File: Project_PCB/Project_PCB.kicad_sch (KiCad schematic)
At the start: 41 parts, among them J1 USB_C_Receptacle, J2 Myoware Connector, J3 Conn_01x02, SW1 SW_Push, SW2 SW_SPST, U1 ESP32-S3-WROOM-1, U2 RT9080-33GJ5, U3 MCP73831T-2ACI/OT, U4 MAX17048G+

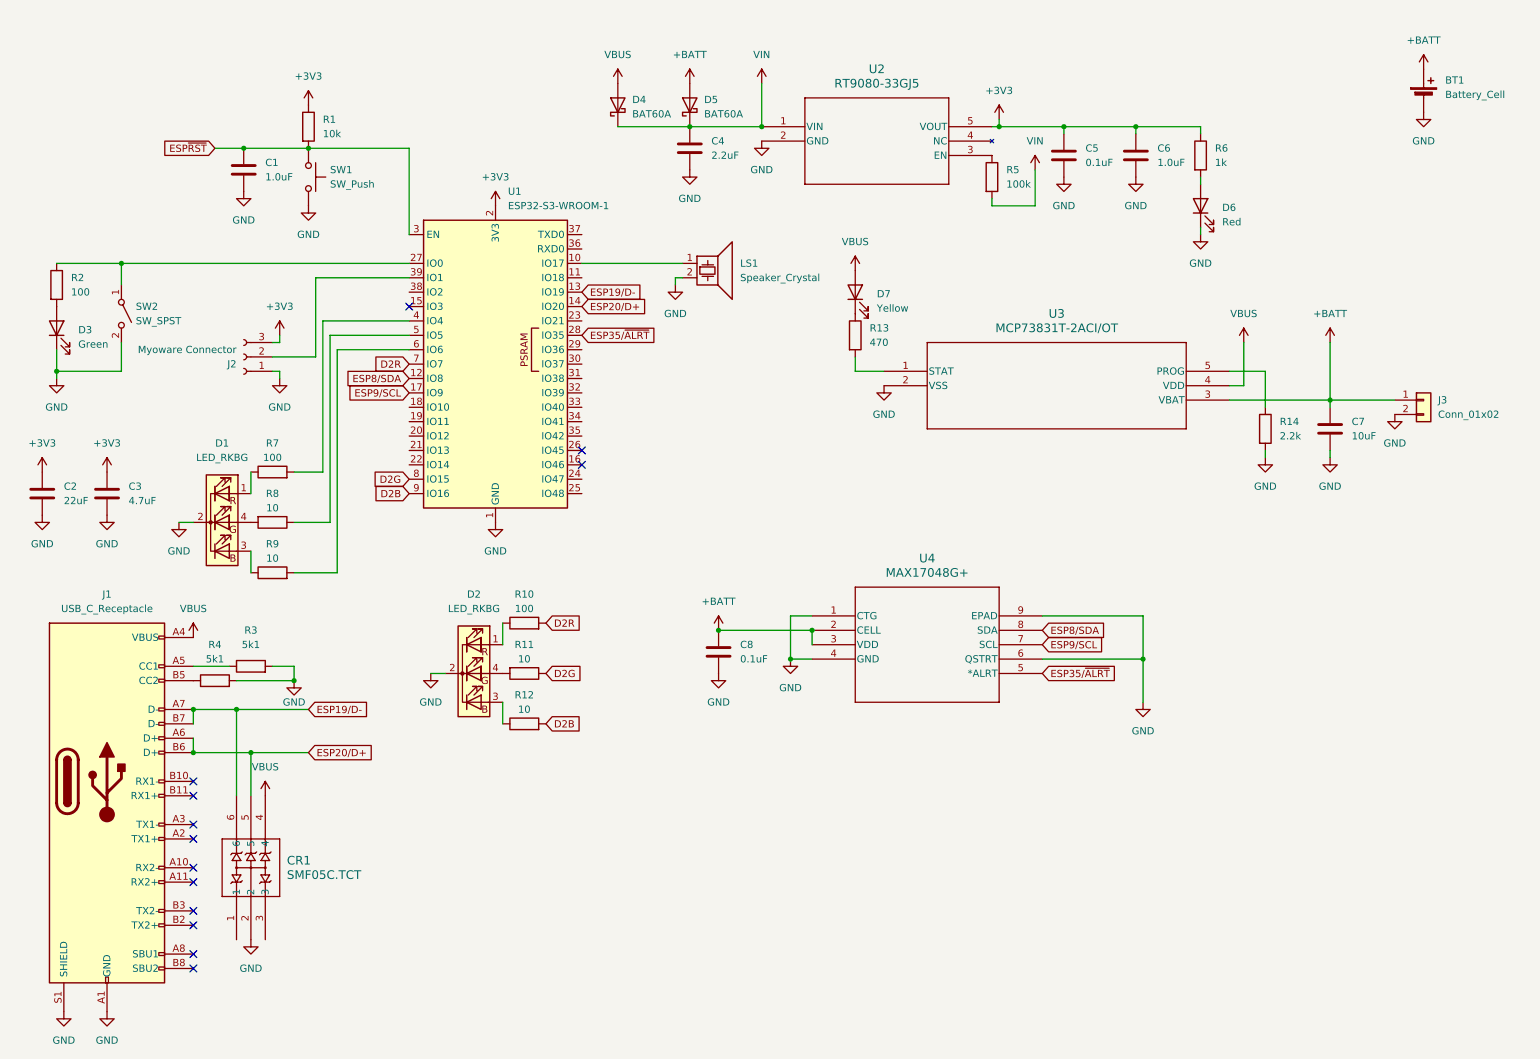
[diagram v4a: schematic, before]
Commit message: Made recommended changes, added some footprints
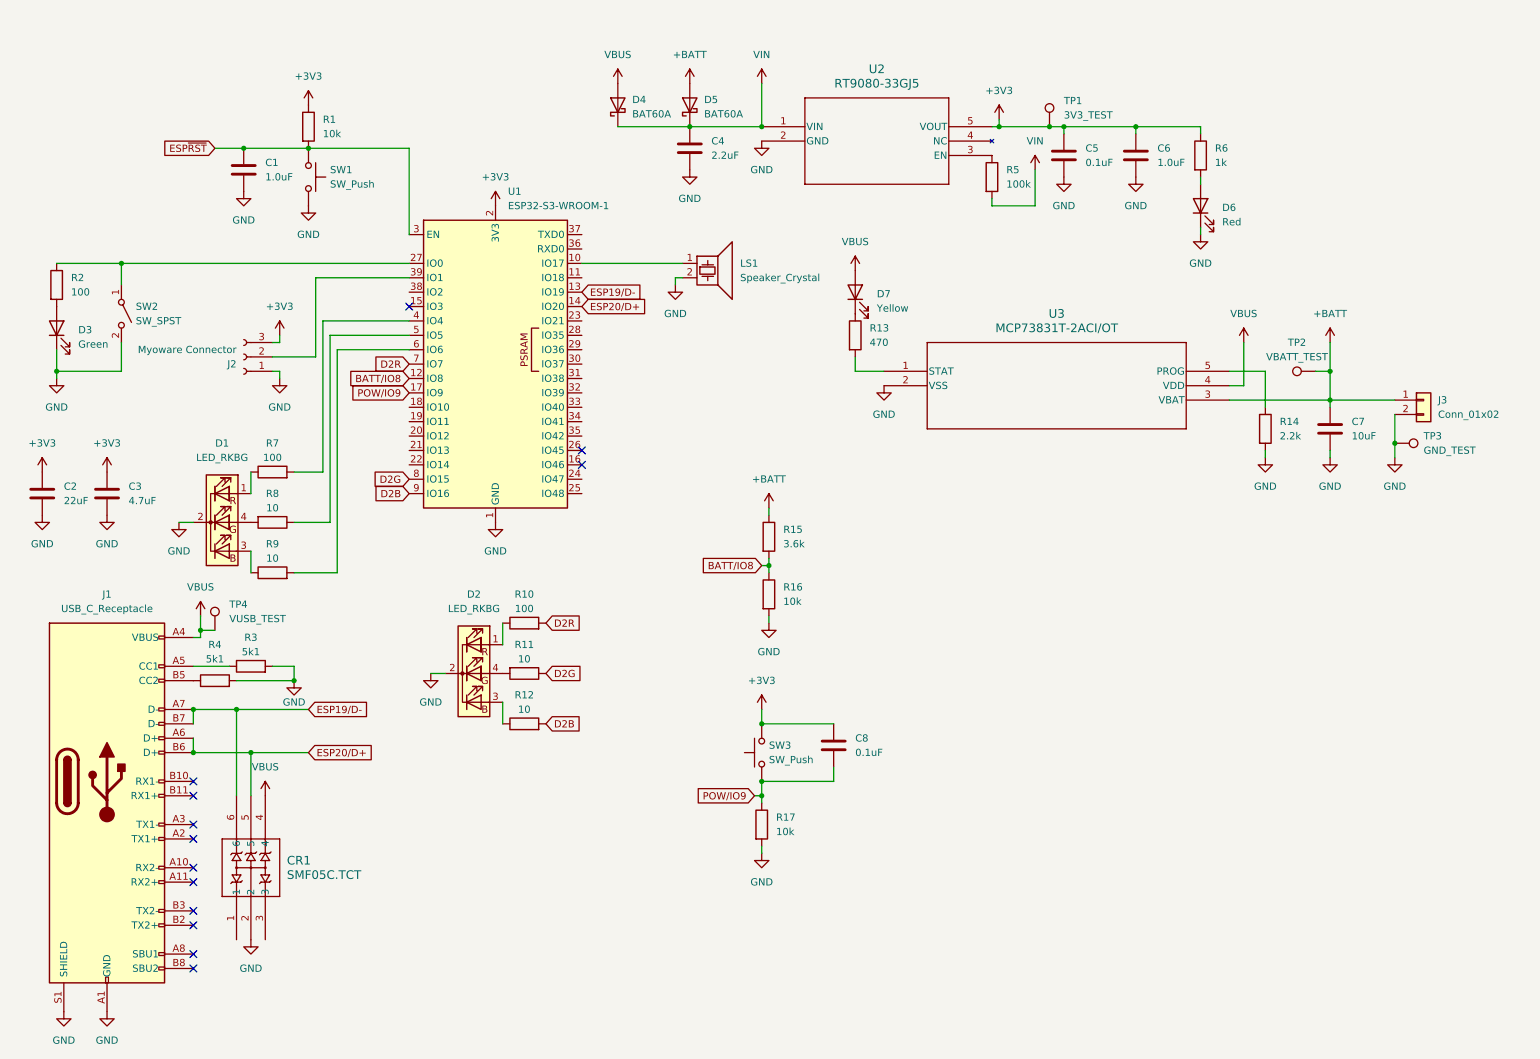
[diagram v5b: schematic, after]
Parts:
- removed BT1: Battery_Cell, symbol Device:Battery_Cell
- removed U4: MAX17048G+, 21-0168_T822+3_MXM, symbol MAX17048G:MAX17048G+
- added R15: 3.6k, Resistor_SMD:R_0603_1608Metric_Pad0.98x0.95mm_HandSolder, symbol Device:R
- added R16, R17: 10k, Resistor_SMD:R_0603_1608Metric_Pad0.98x0.95mm_HandSolder, symbol Device:R
- added SW3: SW_Push, symbol Switch:SW_Push
- added TP1: 3V3_TEST, symbol Connector:TestPoint
- added TP2: VBATT_TEST, symbol Connector:TestPoint
- added TP3: GND_TEST, symbol Connector:TestPoint
- added TP4: VUSB_TEST, symbol Connector:TestPoint
- C1, C5, C6, C8: footprint (none) -> Capacitor_SMD:C_0603_1608Metric_Pad1.08x0.95mm_HandSolder
- CR1: footprint SC70-6L_SEM -> SMF05C:SC70-6L_SEM
- D1, D2: footprint (none) -> LED_THT:LED_D5.0mm-4_RGB
- D3, D6, D7: footprint (none) -> LED_SMD:LED_0805_2012Metric_Pad1.15x1.40mm_HandSolder
- R1, R10, R11, R12, R13, R14, R2, R3, R4, R5, R6, R7, R8, R9: footprint (none) -> Resistor_SMD:R_0603_1608Metric_Pad0.98x0.95mm_HandSolder
- SW1: footprint (none) -> Button_Switch_THT:SW_PUSH_6mm
- U2: footprint TSOT-23-5_RIT -> RT9080:TSOT-23-5_RIT
- U3: footprint SOT-23-5_MC_MCH -> MCP73831:SOT-23-5_MC_MCH
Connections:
- net +3V3: now also C8.1, SW3.2, TP1.1
- net +BATT: now also R15.1, TP2.1; no longer C8.1
- net GND: now also R16.2, R17.2, TP3.1; no longer C8.2
- net VBUS: now also TP4.1
- net ESP35/~{ALRT}: no longer names the net of U1.28 (IO35)
- net ESP8/SDA renamed BATT/IO8
- net BATT/IO8: now also R15.2, R16.1
- net ESP9/SCL renamed POW/IO9
- net POW/IO9: now also C8.2, R17.1, SW3.1

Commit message: Finalized schematic, assigned all footprints
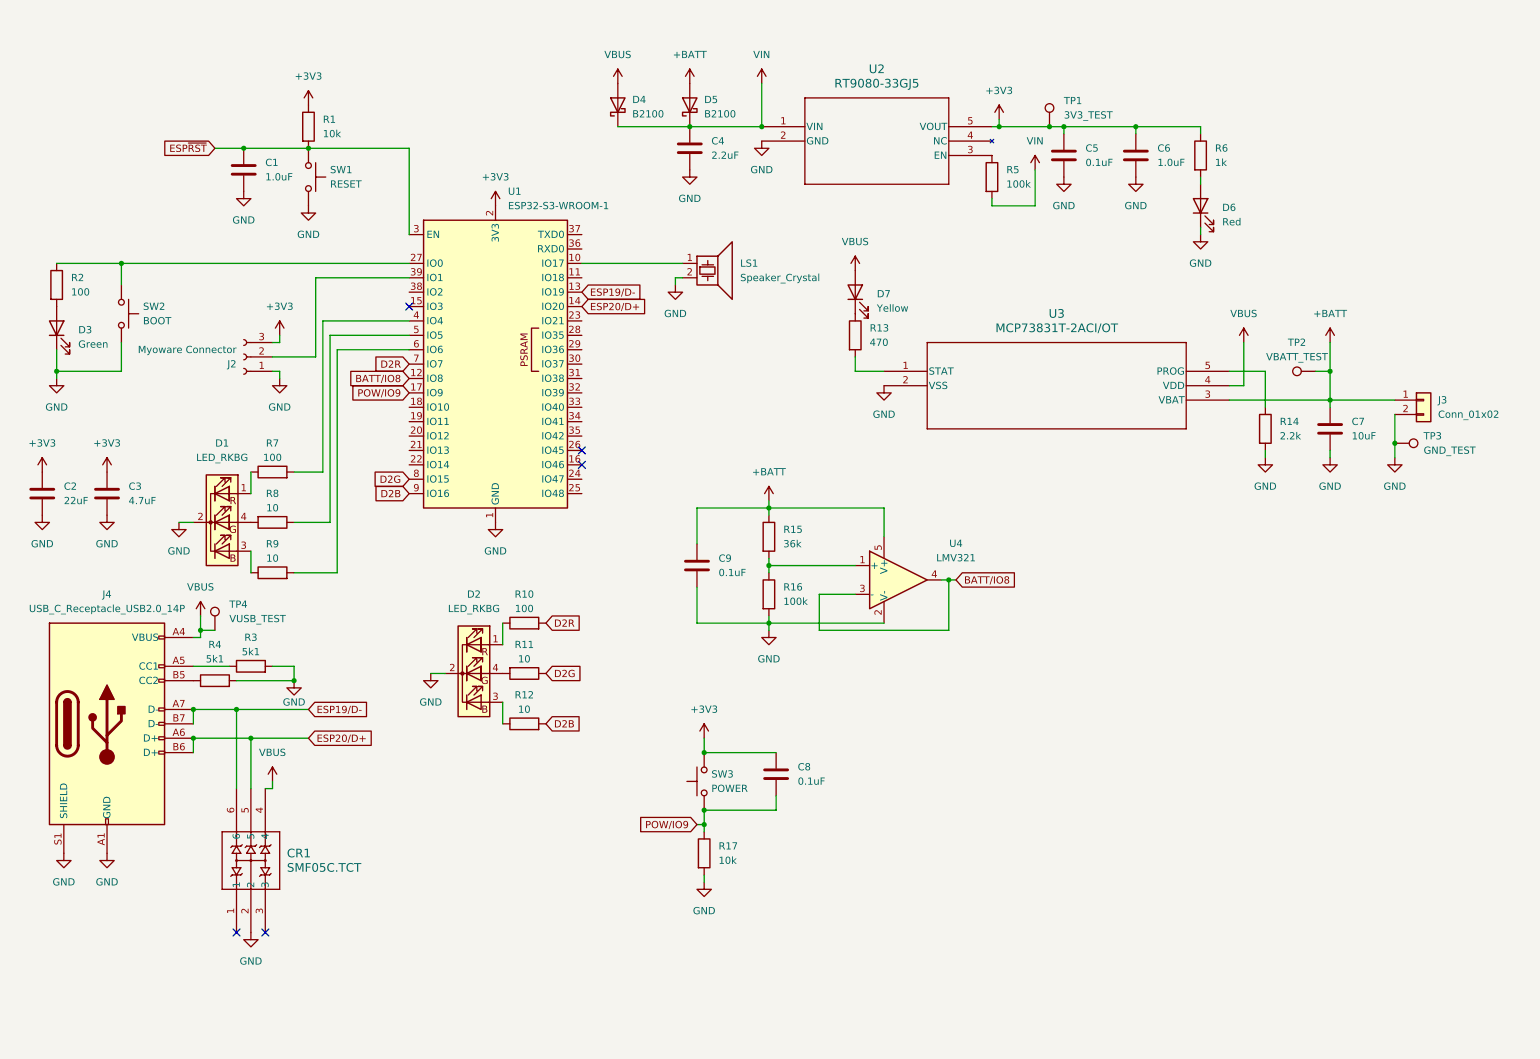
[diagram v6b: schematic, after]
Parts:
- removed D4, D5: BAT60A, Diode_SMD:D_SOD-323, symbol Diode:BAT60A
- removed J1: USB_C_Receptacle, symbol Connector:USB_C_Receptacle
- removed SW2: SW_SPST, symbol Switch:SW_SPST
- added C9: 0.1uF, Capacitor_SMD:C_0603_1608Metric_Pad1.08x0.95mm_HandSolder, symbol Device:C
- added D4, D5: B2100, Diode_SMD:D_SMB_Handsoldering, symbol Device:D_Schottky
- added J4: USB_C_Receptacle_USB2.0_14P, Connector_PinHeader_2.54mm:PinHeader_1x08_P2.54mm_Vertical, symbol Connector:USB_C_Receptacle_USB2.0_14P
- added SW2: BOOT, Button_Switch_SMD:SW_Push_1P1T_NO_CK_KSC6xxJ, symbol Switch:SW_Push
- added U4: LMV321, Package_TO_SOT_SMD:SOT-353_SC-70-5_Handsoldering, symbol Amplifier_Operational:LMV321
- C2: footprint (none) -> Capacitor_THT:C_Radial_D6.3mm_H7.0mm_P2.50mm
- C3, C4, C7: footprint (none) -> Capacitor_THT:C_Radial_D5.0mm_H11.0mm_P2.00mm
- J2: footprint (none) -> Connector_PinHeader_2.54mm:PinHeader_1x03_P2.54mm_Vertical
- LS1: footprint (none) -> LD-BZPN-1705:LDBZPN1705
- R15: value 3.6k -> 36k
- R16: value 10k -> 100k
- SW1: value SW_Push -> RESET; footprint Button_Switch_THT:SW_PUSH_6mm -> Button_Switch_SMD:SW_SPST_PTS647_Sx38
- SW3: value SW_Push -> POWER; footprint (none) -> Connector_PinHeader_2.54mm:PinHeader_1x02_P2.54mm_Vertical
- TP1, TP2, TP3, TP4: footprint (none) -> TestPoint:TestPoint_THTPad_D2.0mm_Drill1.0mm
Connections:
- net +BATT: now also C9.1, D5.2 (A), U4.5 (V+)
- net BATT/IO8: now also U4.3 (-), U4.4; no longer R15.2, R16.1
- net ESP19/D-: now also J4.A7 (D-), J4.B7 (D-)
- net ESP20/D+: now also J4.A6 (D+), J4.B6 (D+)
- net GND: now also C9.2, J4.A1 (GND), J4.A12 (GND), J4.B1 (GND), J4.B12 (GND), J4.S1 (SHIELD), SW2.2, U4.2 (V-)
- net VBUS: now also D4.2 (A), J4.A4 (VBUS), J4.A9 (VBUS), J4.B4 (VBUS), J4.B9 (VBUS)
- net VIN: now also D4.1 (K), D5.1 (K)
- net at R4.1: now also J4.B5 (CC2)
- net at R2.1, U1.27 (IO0): now also SW2.1
- net at R3.1: now also J4.A5 (CC1)
- new net: R15.2, R16.1, U4.1 (+)
- no-connect marks 13 -> 5
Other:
- moved on the sheet: C8, CR1, R17, SW3

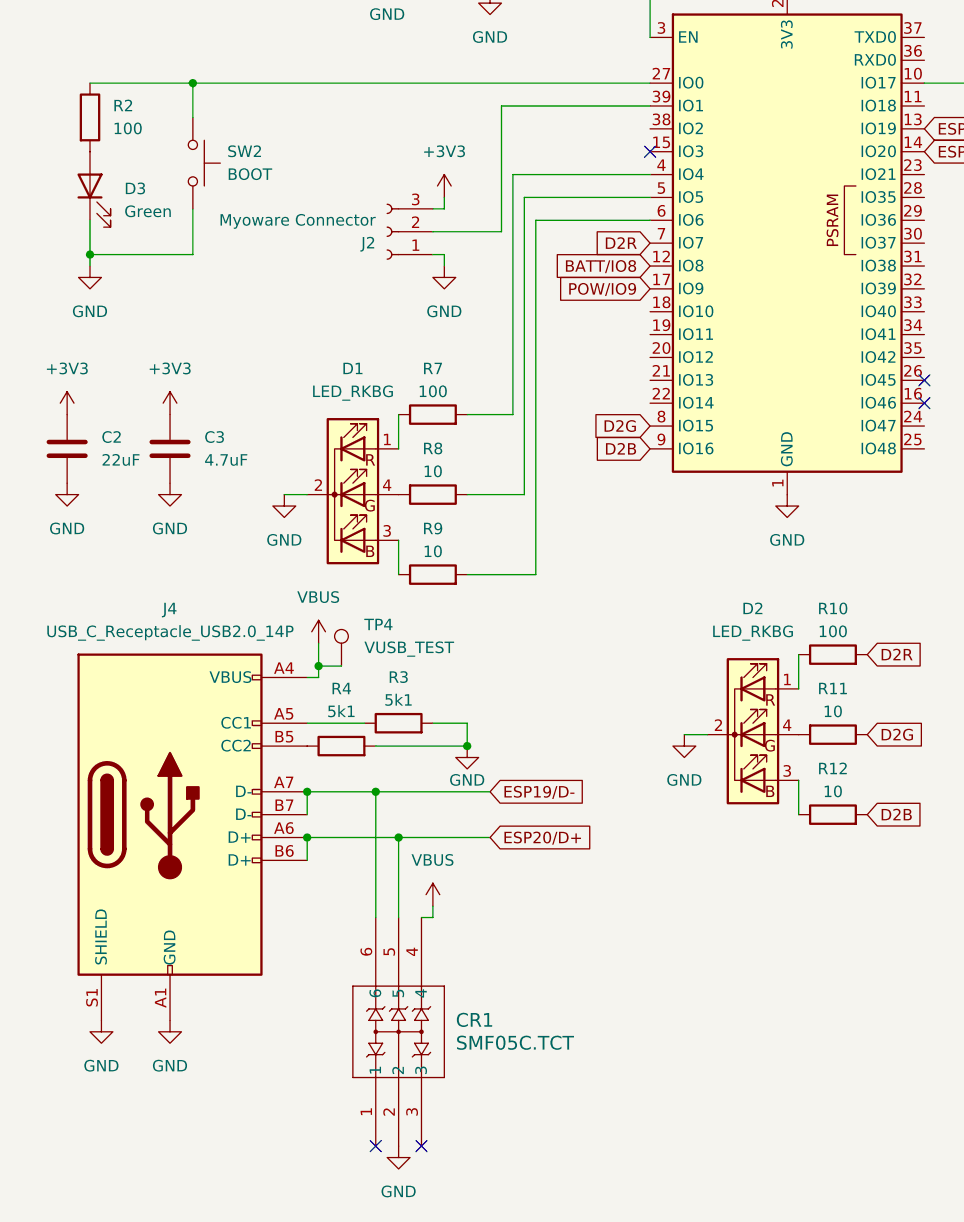
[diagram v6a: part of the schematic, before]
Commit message: Started work on PCB layout, made basic progress
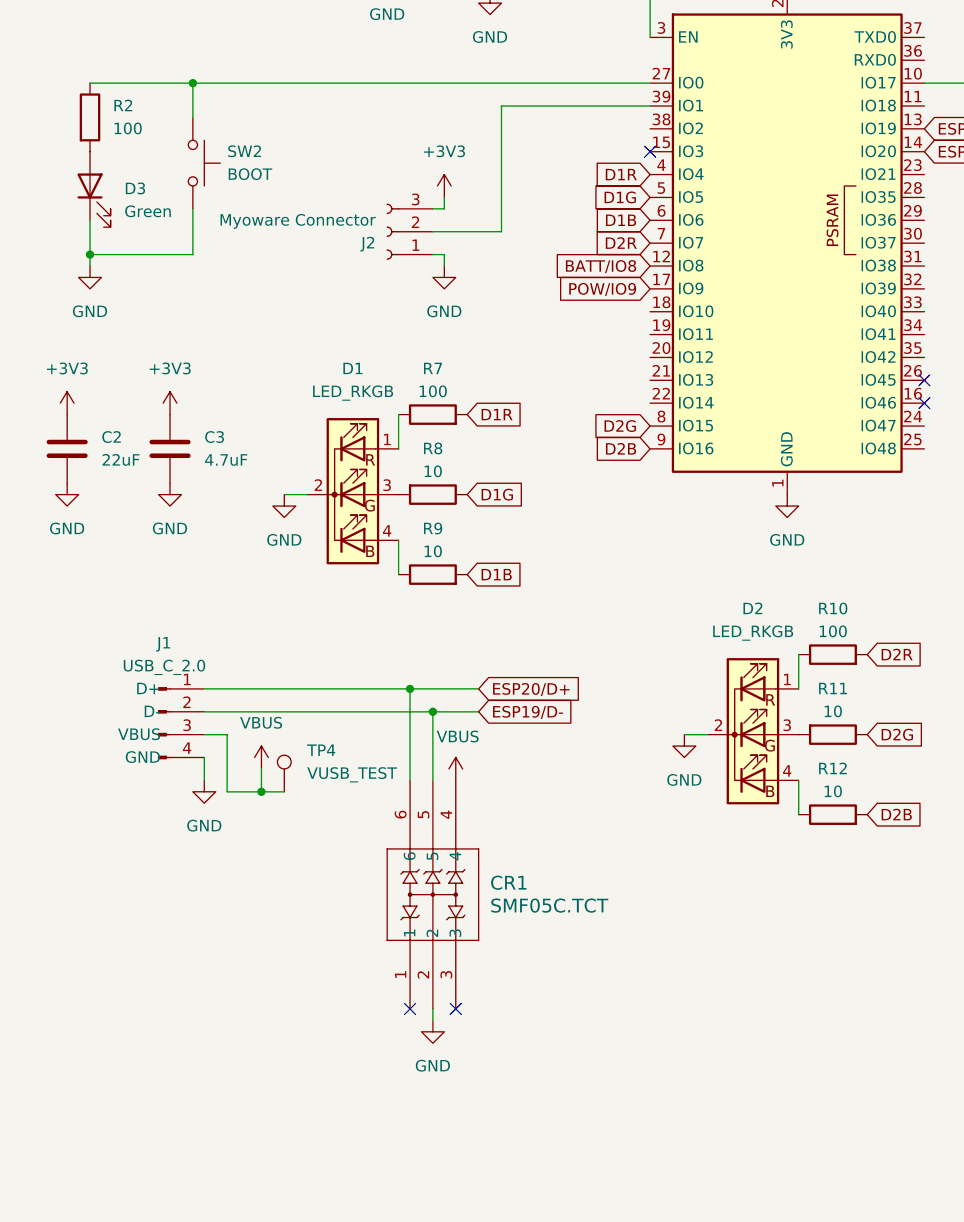
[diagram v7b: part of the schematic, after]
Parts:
- removed D1, D2: LED_RKBG, LED_THT:LED_D5.0mm-4_RGB, symbol Device:LED_RKBG
- removed J4: USB_C_Receptacle_USB2.0_14P, Connector_PinHeader_2.54mm:PinHeader_1x08_P2.54mm_Vertical, symbol Connector:USB_C_Receptacle_USB2.0_14P
- removed R3, R4: 5k1, Resistor_SMD:R_0603_1608Metric_Pad0.98x0.95mm_HandSolder, symbol Device:R
- added D1, D2: LED_RKGB, Connector_PinHeader_2.54mm:PinHeader_1x04_P2.54mm_Vertical, symbol Device:LED_RKGB
- added J1: USB_C_2.0, Connector_PinHeader_2.54mm:PinHeader_1x04_P2.54mm_Vertical, symbol Connector:Conn_01x04_Pin
- J3: footprint Connector_JST:JST_PH_S2B-PH-K_1x02_P2.00mm_Horizontal -> Connector_JST:JST_PH_S2B-PH-SM4-TB_1x02-1MP_P2.00mm_Horizontal
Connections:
- net ESP19/D-: now also CR1.5, J1.2 (D-); no longer CR1.6
- net ESP20/D+: now also CR1.6, J1.1 (D+); no longer CR1.5
- net GND: now also D1.2 (K), D2.2 (K), J1.4 (GND)
- net VBUS: now also J1.3 (VBUS)
- net at R10.1: now also D2.1 (RA)
- net at R11.2: now also D2.3 (GA)
- net D1G: now reaches R8.1, U1.5 (IO5)
- net at R8.2: now also D1.3 (GA)
- net at R7.1: now also D1.1 (RA)
- net D1R: now reaches R7.2, U1.4 (IO4)
- net at R9.1: now also D1.4 (BA)
- net D1B: now reaches R9.2, U1.6 (IO6)
- net at R12.1: now also D2.4 (BA)
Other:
- moved on the sheet: CR1, TP4
